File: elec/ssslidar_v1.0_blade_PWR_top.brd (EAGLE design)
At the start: 12.5 x 7 mm, 24 parts, among them P1 PIN_SMD_0.8X1_RECT, P10 PIN_SMD_0.8X1_RECT, P11 PIN_SMD_1X1_RECT, P12 PIN_SMD_0.8X1_RECT, P13 PIN_SMD_0.8X1_RECT, P14 PIN_SMD_0.8X1_RECT, P16 PIN_SMD_0.8X1_RECT, P17 PIN_SMD_1X1_RECT, P18 PIN_SMD_0.8X1_RECT, P2 PIN_SMD_1X1_RECT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

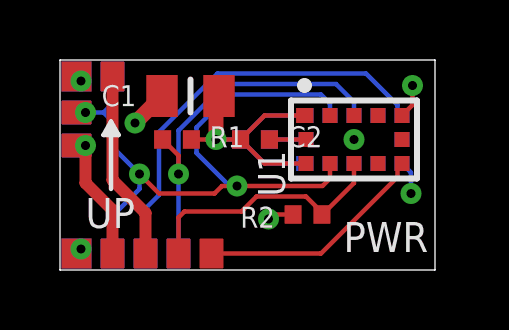
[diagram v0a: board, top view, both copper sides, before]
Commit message: Upadted blade footprint, put everything in v1.0
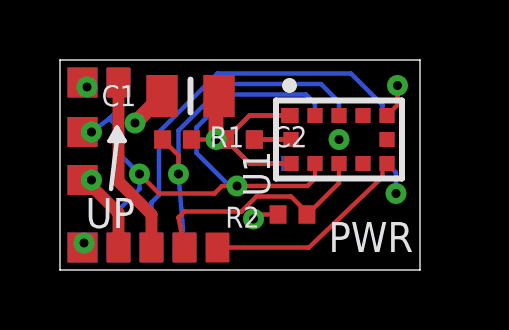
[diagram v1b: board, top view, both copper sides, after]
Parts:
- P10, P12, P13, P16: value PIN_SMD_0.8X1_RECT -> PIN_SMD_1X1_RECT; device Xevelabs:PIN_SMD_0.8X1_RECT -> Xevelabs:PIN_SMD_1X1_RECT
- moved P13 1.17 mm to (0.75, 3.00)
- moved P16 1.17 mm to (0.75, 3.00)
- moved P10 0.68 mm to (0.75, 4.60)
- moved P12 0.68 mm to (0.75, 4.60)
- moved C2 0.50 mm to (6.00, 4.35)
- moved C3 0.50 mm to (6.00, 4.35)
- moved R2 0.50 mm to (7.75, 1.85)
- moved U1 0.50 mm to (9.30, 4.35)
- moved U2 0.50 mm to (9.30, 4.35)
- moved P1 0.28 mm to (1.95, 6.25)
- moved P18 0.28 mm to (1.95, 6.25)
- moved P2 0.28 mm to (0.75, 6.25)
- moved P4 0.28 mm to (4.15, 0.75)
- moved P5 0.28 mm to (4.15, 0.75)
- moved P6 0.28 mm to (5.25, 0.75)
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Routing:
- net VDD: track 22.0 -> 19.6 mm
- net SCL: track 23.5 -> 22.1 mm
- net INT1: track 7.77 -> 6.96 mm
- net INT2: track 14.0 -> 13.3 mm
- net SDA1: track 8.71 -> 8.03 mm
- net SDA2: track 12.9 -> 12.2 mm
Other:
- board size 12.5 x 7 mm -> 12 x 7 mm

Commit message: Separated blades into bottom and top, since the bottom ones need to be taller to avoid seeing the Main PCB, or the screws...
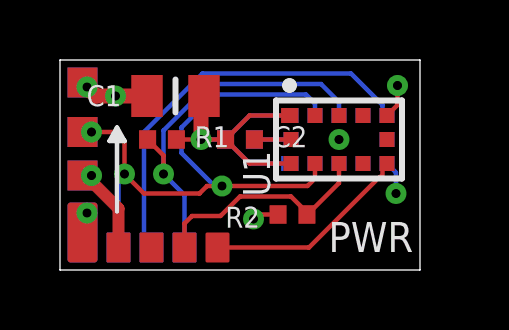
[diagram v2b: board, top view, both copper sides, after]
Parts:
- removed P1, P18: PIN_SMD_0.8X1_RECT, Xevelabs:PIN_SMD_0.8X1_RECT
- P11, P17: value PIN_SMD_1X1_RECT -> PIN_SMD_1X2; device Xevelabs:PIN_SMD_1X1_RECT -> Xevelabs:PIN_SMD_1X2
- moved P11 0.50 mm to (0.75, 1.25), turned to 180 degrees
- moved P17 0.50 mm to (0.75, 1.25), turned to 0 degrees
- moved R1 0.50 mm to (3.40, 4.35)
- moved C1 0.50 mm to (3.85, 5.80)
- moved P13 0.15 mm to (0.75, 3.15)
- moved P16 0.15 mm to (0.75, 3.15)
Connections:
- removed net VDD_PASS: P1.PIN, P14.PIN
- net GND: now also P11.P$1, P17.P$1; no longer P11.PIN, P17.PIN
- net SCL: no longer P18.PIN
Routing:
- net VDD_PASS: track 5.96 -> 0.00 mm
- net GND: track 4.60 -> 6.41 mm
- net SCL: track 22.1 -> 20.9 mm
- net VDD: track 19.6 -> 20.8 mm
- net SDA2: track 12.2 -> 12.8 mm
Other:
- board text removed: "UP"

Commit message: Updated all libs.
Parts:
- turned P11 to 270 degrees
- turned P17 to 270 degrees
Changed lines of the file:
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@@
 <element name="P7" library="Xevelabs" package="PIN_SMD_0.8X1_RECT" value="PIN_SMD_0.8X1_RECT" x="3.05" y="0.75" rot="MR90"/>
 <element name="P16" library="Xevelabs" package="PIN_SMD_1X1_RECT" value="PIN_SMD_1X1_RECT" x="0.75" y="3.15" rot="R180"/>
-<element name="P17" library="Xevelabs" package="PIN_SMD_1X2" value="PIN_SMD_1X2" x="0.75" y="1.25" rot="MR0"/>
+<element name="P17" library="Xevelabs" package="PIN_SMD_1X2" value="PIN_SMD_1X2" x="0.75" y="1.25" rot="MR270"/>
 <element name="P8" library="Xevelabs" package="PIN_SMD_0.8X1_RECT" value="PIN_SMD_0.8X1_RECT" x="1.95" y="0.75" rot="R90"/>
 <element name="P9" library="Xevelabs" package="PIN_SMD_1X1_RECT" value="PIN_SMD_1X1_RECT" x="0.75" y="6.25"/>
 <element name="P10" library="Xevelabs" package="PIN_SMD_1X1_RECT" value="PIN_SMD_1X1_RECT" x="0.75" y="4.6" rot="MR180"/>
-<element name="P11" library="Xevelabs" package="PIN_SMD_1X2" value="PIN_SMD_1X2" x="0.75" y="1.25" rot="R180"/>
+<element name="P11" library="Xevelabs" package="PIN_SMD_1X2" value="PIN_SMD_1X2" x="0.75" y="1.25" rot="R270"/>
 <element name="P12" library="Xevelabs" package="PIN_SMD_1X1_RECT" value="PIN_SMD_1X1_RECT" x="0.75" y="4.6"/>
 <element name="P13" library="Xevelabs" package="PIN_SMD_1X1_RECT" value="PIN_SMD_1X1_RECT" x="0.75" y="3.15" rot="MR0"/>
